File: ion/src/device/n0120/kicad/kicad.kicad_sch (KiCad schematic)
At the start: 6 parts, among them Q4 2N7002, U1 STM32H725VETx, U5 AT25SF641

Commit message: added led to schematic
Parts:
- added LD1: LED_ARGB, symbol Device:LED_ARGB
- added Q1, Q2, Q3: 2N7002, Package_TO_SOT_SMD:SOT-23, symbol Transistor_FET:2N7002
- added R6, R7, R8: R, symbol Device:R
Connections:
- net GND: now also Q1.2 (S), Q2.2 (S), Q3.2 (S)
- net led_blue: now reaches U1.64 (PC8)
- net led_blue: now also Q3.1 (G)
- net led_red: now reaches U1.90 (PB4(NJTRST))
- net led_red: now also Q1.1 (G)
- net led_green: now reaches U1.91 (PB5)
- net led_green: now also Q2.1 (G)
- new net: Q1.3 (D), R6.1
- new net: LD1.2 (RK), R6.2
- new net: LD1.3 (GK), R7.2
- new net: LD1.4 (BK), R8.2
- new net: Q3.3 (D), R8.1
- new net: Q2.3 (D), R7.1
- new net vbat: LD1.1 (A)
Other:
- note added: "external flash"
- note added: "led rgb"
- moved on the sheet: C22, Q4, R10, R9, U1, U5

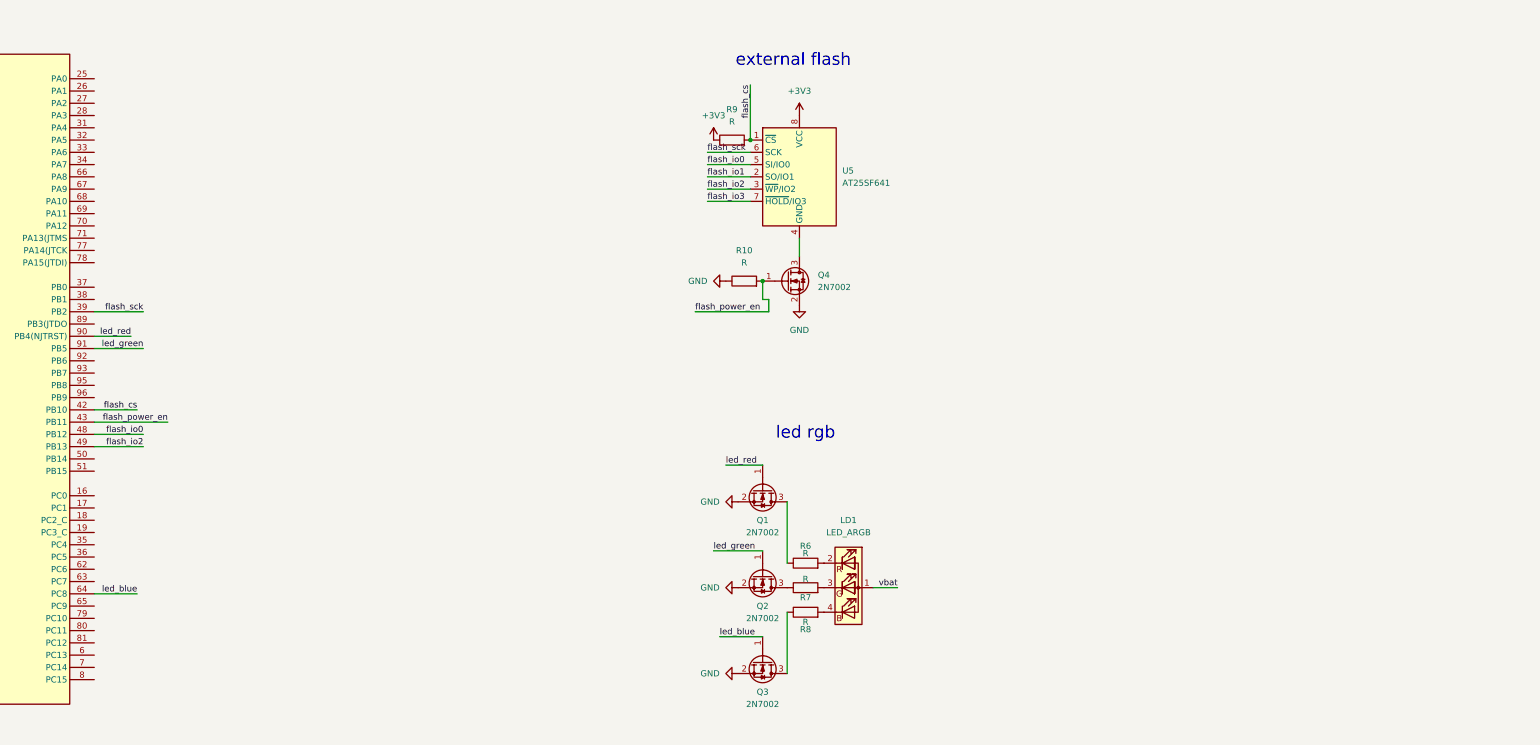
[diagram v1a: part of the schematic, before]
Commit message: added keyboard to schematic
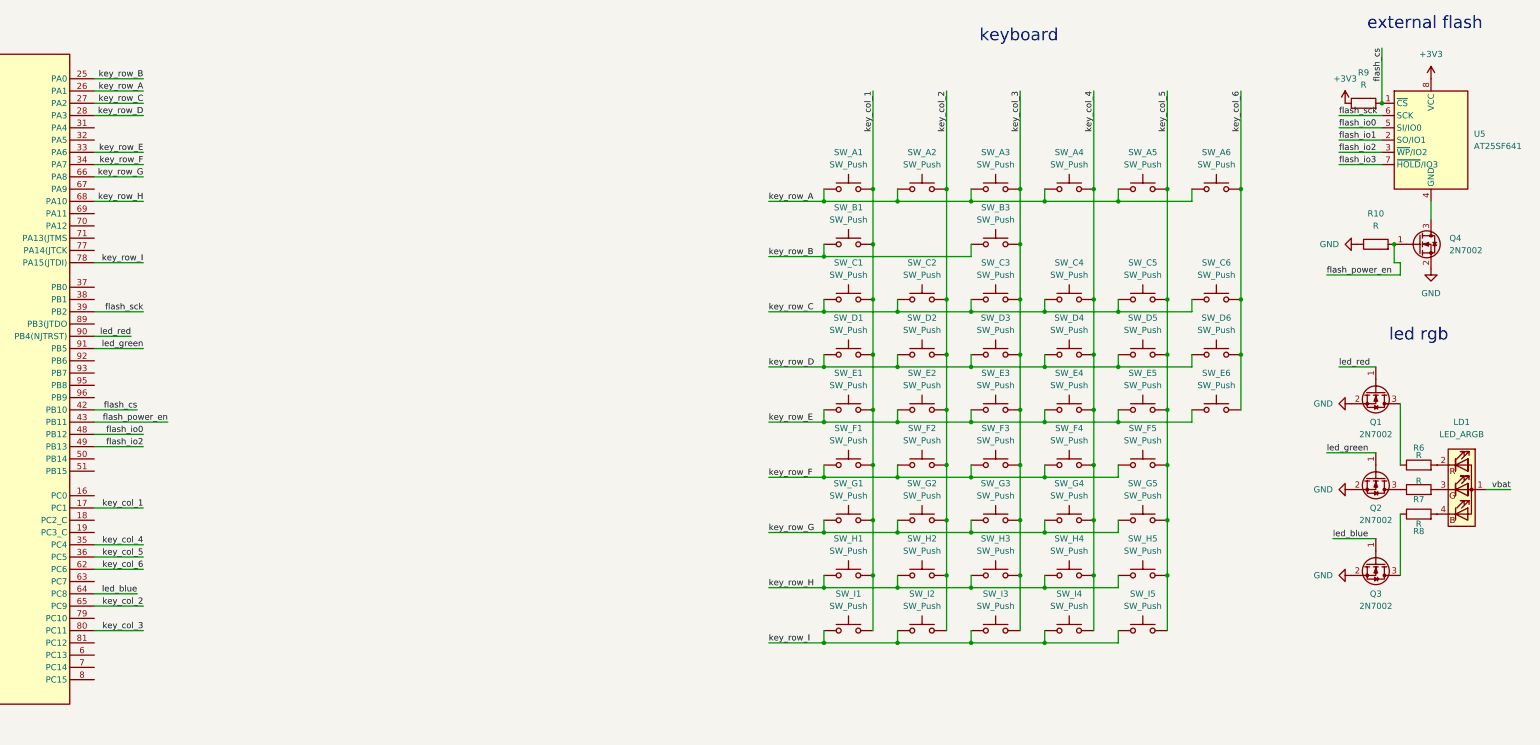
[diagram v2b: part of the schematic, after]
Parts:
- added SW_A1, SW_A2, SW_A3, SW_A4, SW_A5, SW_A6, SW_B1, SW_B3, SW_C1, SW_C2, SW_C3, SW_C4, SW_C5, SW_C6, SW_D1, SW_D2, SW_D3, SW_D4, SW_D5, SW_D6, SW_E1, SW_E2, SW_E3, SW_E4, SW_E5, SW_E6, SW_F1, SW_F2, SW_F3, SW_F4, SW_F5, SW_G1, SW_G2, SW_G3, SW_G4, SW_G5, SW_H1, SW_H2, SW_H3, SW_H4, SW_H5, SW_I1, SW_I2, SW_I3, SW_I4, SW_I5: SW_Push, symbol Switch:SW_Push
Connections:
- net key_col_1: now reaches U1.17 (PC1)
- net key_col_1: now also SW_A1.2, SW_B1.2, SW_C1.2, SW_D1.2, SW_E1.2, SW_F1.2, SW_G1.2, SW_H1.2, SW_I1.2
- net key_row_B: now reaches U1.25 (PA0)
- net key_row_B: now also SW_B1.1, SW_B3.1
- net key_row_A: now reaches U1.26 (PA1)
- net key_row_A: now also SW_A1.1, SW_A2.1, SW_A3.1, SW_A4.1, SW_A5.1, SW_A6.1
- net key_row_C: now reaches U1.27 (PA2)
- net key_row_C: now also SW_C1.1, SW_C2.1, SW_C3.1, SW_C4.1, SW_C5.1, SW_C6.1
- net key_row_D: now reaches U1.28 (PA3)
- net key_row_D: now also SW_D1.1, SW_D2.1, SW_D3.1, SW_D4.1, SW_D5.1, SW_D6.1
- net key_row_E: now reaches U1.33 (PA6)
- net key_row_E: now also SW_E1.1, SW_E2.1, SW_E3.1, SW_E4.1, SW_E5.1, SW_E6.1
- net key_row_F: now reaches U1.34 (PA7)
- net key_row_F: now also SW_F1.1, SW_F2.1, SW_F3.1, SW_F4.1, SW_F5.1
- net key_col_4: now reaches U1.35 (PC4)
- net key_col_4: now also SW_A4.2, SW_C4.2, SW_D4.2, SW_E4.2, SW_F4.2, SW_G4.2, SW_H4.2, SW_I4.2
- net key_col_5: now reaches U1.36 (PC5)
- net key_col_5: now also SW_A5.2, SW_C5.2, SW_D5.2, SW_E5.2, SW_F5.2, SW_G5.2, SW_H5.2, SW_I5.2
- net key_col_6: now reaches U1.62 (PC6)
- net key_col_6: now also SW_A6.2, SW_C6.2, SW_D6.2, SW_E6.2
- net key_col_2: now reaches U1.65 (PC9)
- net key_col_2: now also SW_A2.2, SW_C2.2, SW_D2.2, SW_E2.2, SW_F2.2, SW_G2.2, SW_H2.2, SW_I2.2
- net key_row_G: now reaches U1.66 (PA8)
- net key_row_G: now also SW_G1.1, SW_G2.1, SW_G3.1, SW_G4.1, SW_G5.1
- net key_row_H: now reaches U1.68 (PA10)
- net key_row_H: now also SW_H1.1, SW_H2.1, SW_H3.1, SW_H4.1, SW_H5.1
- net key_row_I: now reaches U1.78 (PA15(JTDI))
- net key_row_I: now also SW_I1.1, SW_I2.1, SW_I3.1, SW_I4.1, SW_I5.1
- net key_col_3: now reaches U1.80 (PC11)
- net key_col_3: now also SW_A3.2, SW_B3.2, SW_C3.2, SW_D3.2, SW_E3.2, SW_F3.2, SW_G3.2, SW_H3.2, SW_I3.2
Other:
- note added: "keyboard"
- moved on the sheet: LD1, Q1, Q2, Q3, Q4, R10, R6, R7, R8, R9, U5
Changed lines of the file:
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@@
 	(generator "eeschema")
 	(generator_version "9.0")
-	(paper "A4")
+	(paper "A3")
